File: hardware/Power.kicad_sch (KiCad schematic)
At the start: 18 parts, among them K8 G5V-2-DC12, U10 V7805-1000

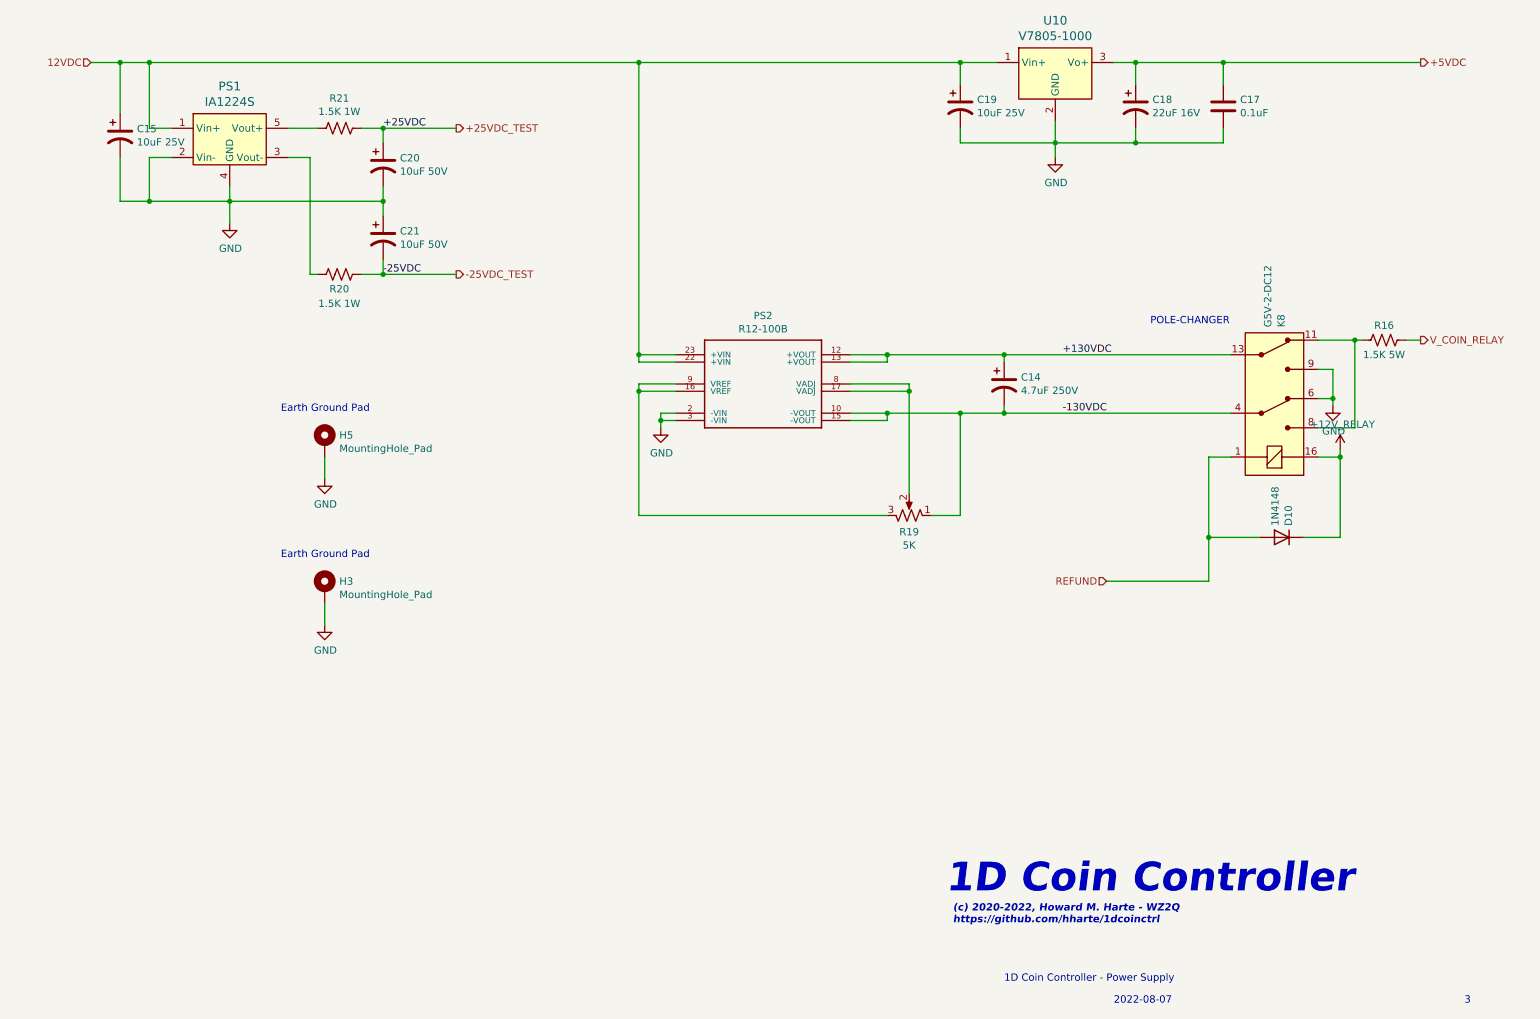
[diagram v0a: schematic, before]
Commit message: Issue 4: Switch from PIC to AVR128DA28 MCU.
    * The AVR128DA28 is supported by the Arduino IDE.
    * Simpler UPDI programming.
    * Update to KiCAD 8.0.1
    * Fix footprint outline for IA1224S DC-DC converter.
    * Add initial Arduino firmware for AVR128DA28 MCU.
    * Move Earth Ground hole.
    * Add jumpers for UART and UPDI configuration.
    * Add 3D-printable end caps for Hammond enclosure.
    * Geographical reannotate PCB.
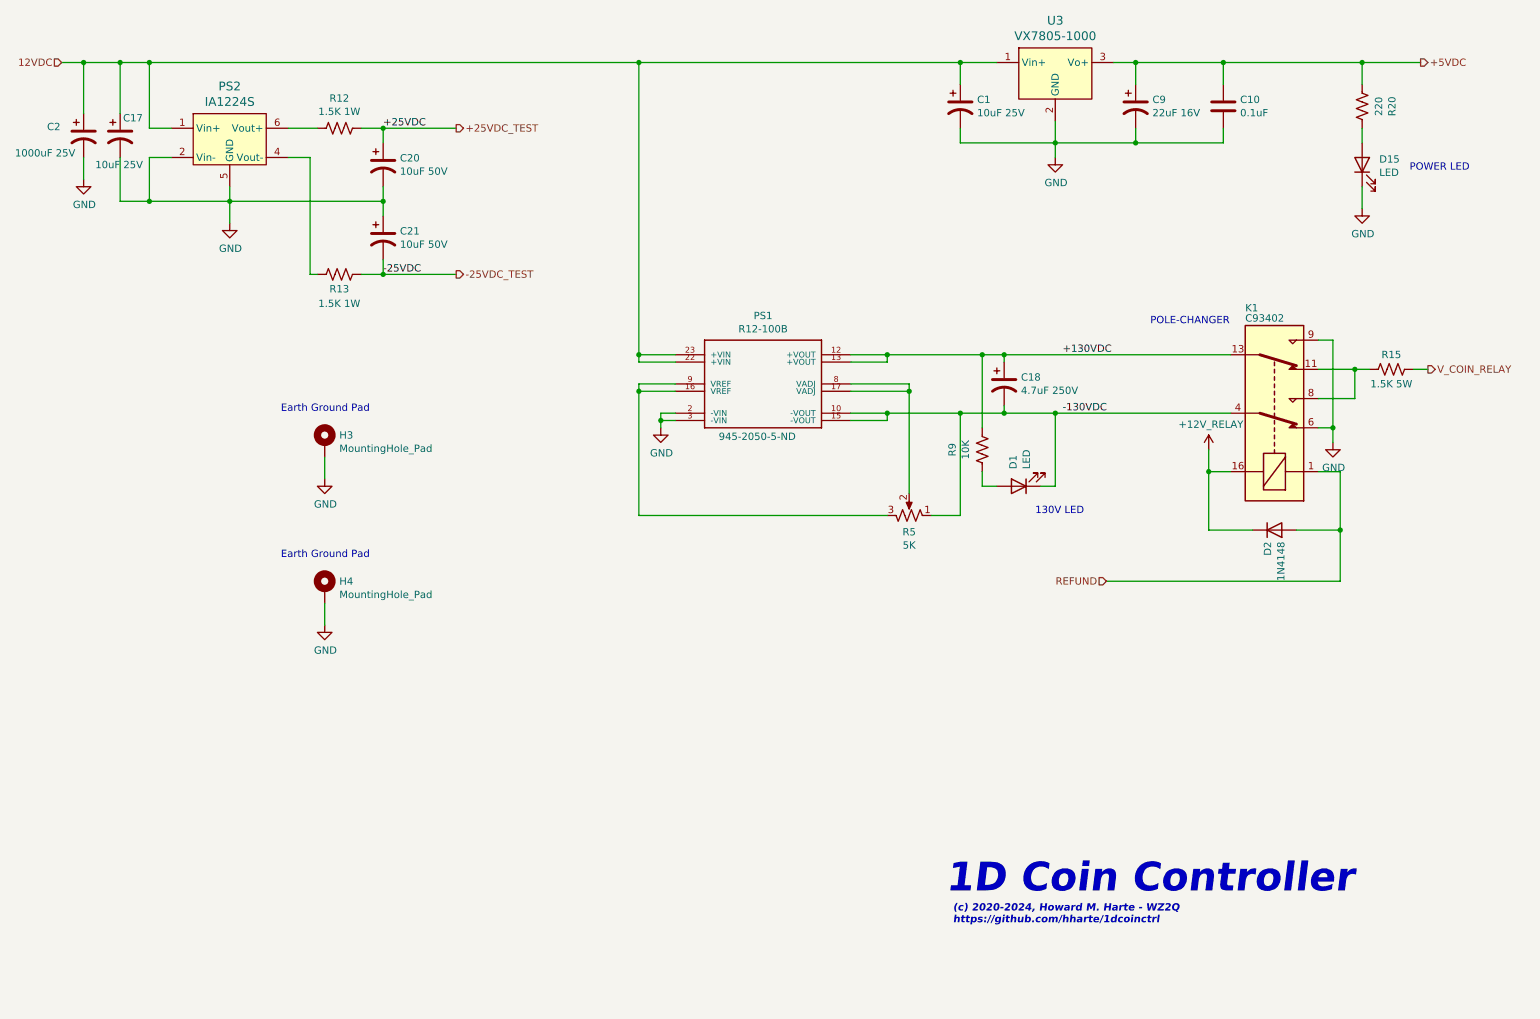
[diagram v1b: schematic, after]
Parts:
- added C2: 1000uF 25V, Capacitor_THT:CP_Radial_D12.5mm_P5.00mm, symbol Device:C_Polarized_US
- added D1, D15: LED, LED_THT:LED_D5.0mm, symbol Device:LED
- added R20: 220, Resistor_THT:R_Axial_DIN0207_L6.3mm_D2.5mm_P7.62mm_Horizontal, symbol Device:R_US
- added R9: 10K, Resistor_THT:R_Axial_DIN0207_L6.3mm_D2.5mm_P7.62mm_Horizontal, symbol Device:R_US
- C1: renamed from C19; Digi-Key_PN (none) -> 445-180683-1-ND; MPN (none) -> FA26X7R1E106KRU06
- C10: renamed from C17; Digi-Key_PN (none) -> 56-K104M15X7RF5TL2CT-ND; MPN (none) -> K104M15X7RF5TL2
- C17: renamed from C15; Digi-Key_PN (none) -> 445-180683-1-ND; MPN (none) -> FA26X7R1E106KRU06
- C18: renamed from C14; Digi-Key_PN (none) -> 338-2361-ND; MPN (none) -> SEK4R7M250ST
- C20, C21: Digi-Key_PN (none) -> P19534CT-ND; MPN (none) -> ECA-1JM100I
- C9: renamed from C18; Digi-Key_PN (none) -> 445-FK20X7R1C226MR000-ND; MPN (none) -> FK20X7R1C226MR000
- D2: renamed from D10; Digi-Key_PN (none) -> 1N4148TACT-ND; MPN (none) -> 1N4148TA
- H3: renamed from H5; now left out of the parts list
- H4: renamed from H3; now left out of the parts list
- K1: renamed from K8; value G5V-2-DC12 -> C93402; footprint digikey-footprints:Relay_THT_G5V-2 -> Relay_THT:Relay_DPDT_Omron_G5V-2; symbol 1d_coinctrl_r2-rescue:G5V-2-DC12-dk_Signal-Relays-Up-to-2-Amps -> Relay:G5V-2; DK_Datasheet_Link http://omronfs.omron.com/en_US/ecb/products/pdf/en-g5v_2.pdf -> https://omronfs.omron.com/en_US/ecb/products/pdf/en-g5v_2.p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; MPN G5V-2-DC12 -> C93402
- PS1: renamed from PS2; footprint kicad-snapeda:CONV_R12-100B -> 1dcoinctrl:CONV_R12-100B; Digi-Key_PN (none) -> 945-2050-5-ND; MPN (none) -> R12-100B
- PS2: renamed from PS1; footprint 1dcoinctrl_r2:IA1224S -> 1dcoinctrl:IA1224S; DK_Datasheet_Link https://www.cui.com/product/resource/digikeypdf/v78-500.pdf -> https://www.xppower.com/portals/0/pdfs/SF_IA.pdf; DK_Detail_Page /product-detail/en/cui-inc/V7805-500/102-1709-ND/1828602 -> https://www.digikey.com/en/products/detail/xp-power/IA1224S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; Digi-Key_PN 102-1709-ND -> 1470-1364-5-ND; MPN V7805-500 -> IA1224S; Manufacturer CUI Inc. -> XP Power
- R12: renamed from R21; Digi-Key_PN (none) -> PPC1.5KW-1CT-ND; MPN (none) -> PR01000101501JR500
- R13: renamed from R20; Digi-Key_PN (none) -> PPC1.5KW-1CT-ND; MPN (none) -> PR01000101501JR500
- R15: renamed from R16; Digi-Key_PN (none) -> A131371CT-ND; MPN (none) -> EP5WS1K5J
- R5: renamed from R19; Digi-Key_PN (none) -> 987-1067-ND; MPN (none) -> 64WR5KLF
- U3: renamed from U10; value V7805-1000 -> VX7805-1000; footprint digikey-footprints:3-SIP_Module_V7805-1000 -> 1dcoinctrl:VX7805-1000; Digi-Key_PN 102-1715-ND -> 102-4253-ND; MPN V7805-1000 -> VX7805-1000
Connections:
- net +130VDC: now also R9.1
- net +5VDC: now also R20.2
- net -130VDC: now also D1.1 (K)
- net 12VDC: now also C2.1
- net GND: now also PS2.5 (GND), C2.2, D15.1 (K); no longer PS2.4 (GND)
- net at R13.2: now also PS2.4 (Vout-); no longer PS2.3 (Vout-)
- net at R12.2: now also PS2.6 (Vout+); no longer PS2.5 (Vout+)
- new net: D1.2 (A), R9.2
- new net: D15.2 (A), R20.1
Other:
- note added: "(c) 2020-2024, Howard M. Harte - WZ2Q https://github.com/hharte/1dcoinctrl"
- note added: "130V LED"
- note added: "POWER LED"
- note removed: "(c) 2020-2022, Howard M. Harte - WZ2Q https://github.com/hharte/1dcoinctrl"
- note removed: "1D Coin Controller - Power Supply"
- note removed: "2022-08-07"
- note removed: "3"
- title: (none) -> 1D Coin Controller - Power Supply
- moved on the sheet: D2, R15
